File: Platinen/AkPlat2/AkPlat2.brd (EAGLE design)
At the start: 54.6 x 46.6 mm, 12 parts, among them CON1 XT30UPB-M, X1 332-02, X2 332-02, X3 332-02, X4 332-02

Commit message: platine verbessert
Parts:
- removed X1, X2, X3, X4: 332-02, con-garry:332-02
- added SV1, SV2: (no value), con-lstb:MA04-1
- moved JP4 1.38 mm to (4.60, 10.3)
- moved JP3 0.64 mm to (4.58, 17.9)
- moved JP1 0.58 mm to (4.58, 33.2)
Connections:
- net N$16: now also SV1.1; no longer X1.2
- net N$17: now also SV1.2; no longer X1.1
- net N$18: now also SV1.3; no longer X2.2
- net N$19: now also SV1.4; no longer X2.1
- net N$20: now also SV2.1; no longer X3.2
- net N$21: now also SV2.2; no longer X3.1
- net N$22: now also SV2.3; no longer X4.2
- net N$23: now also SV2.4; no longer X4.1
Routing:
- net N$8: track 48.7 -> 51.7 mm
- net N$27: track 9.62 -> 7.51 mm
- net N$24: track 103.7 -> 105.3 mm
- net N$9: track 16.6 -> 18.1 mm
- net N$11: track 22.6 -> 24.0 mm
- net N$18: track 4.32 -> 5.47 mm
- net N$23: track 3.81 -> 4.88 mm
- net N$20: track 4.50 -> 5.53 mm
- net N$17: track 4.81 -> 5.76 mm
- net N$19: track 4.83 -> 5.76 mm
- net N$16: track 4.31 -> 5.18 mm
- net N$28: track 159.1 -> 158.2 mm
- net N$21: track 3.99 -> 4.81 mm
- net N$22: track 3.91 -> 4.53 mm
- net N$7: track 8.90 -> 8.33 mm
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
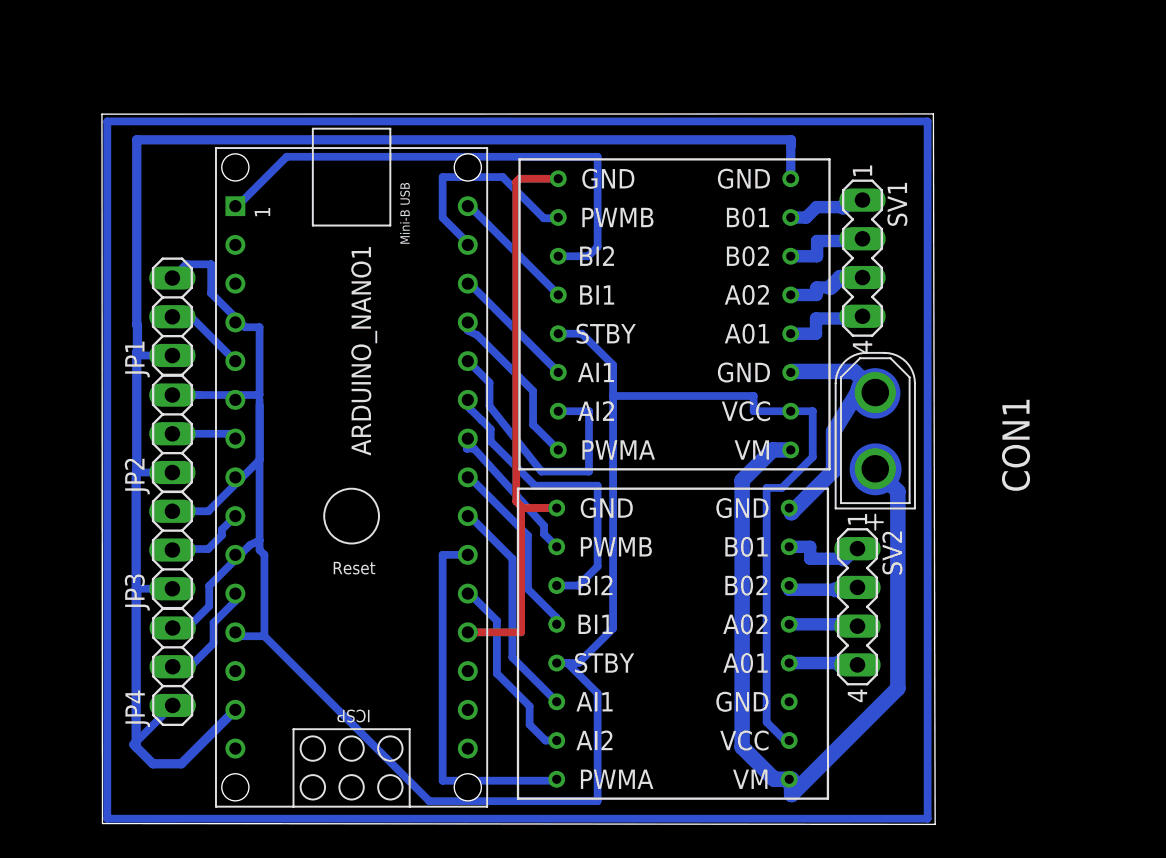
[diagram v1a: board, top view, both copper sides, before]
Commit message: Platine changes and smother movement
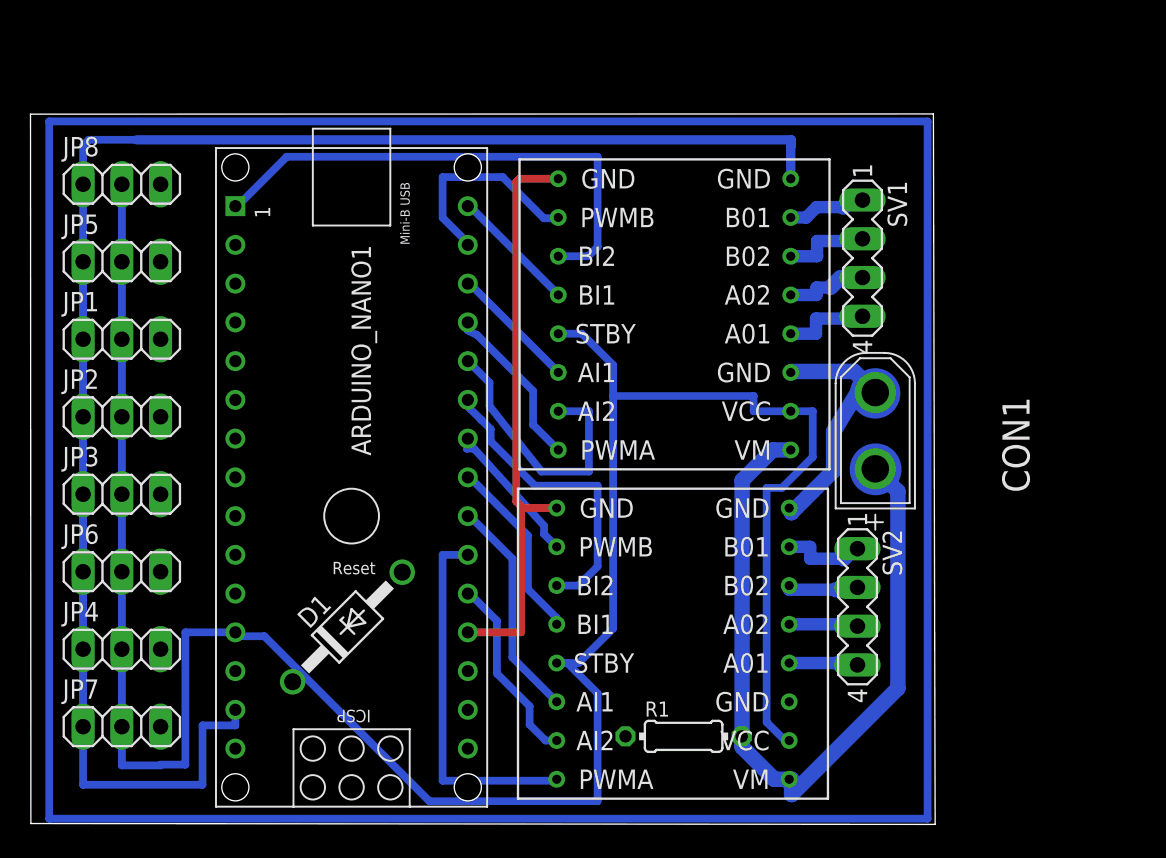
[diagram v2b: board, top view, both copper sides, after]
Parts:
- added D1: BZX85, diode:DO41Z10
- added JP5, JP6, JP7, JP8: (no value), pinhead:1X03
- added R1: (no value), rcl:0204/7
- moved JP3 4.94 mm to (1.27, 21.6), turned to 0 degrees
- moved JP1 3.63 mm to (1.27, 31.8), turned to 0 degrees
- moved JP4 3.53 mm to (1.27, 11.4), turned to 0 degrees
- moved JP2 3.50 mm to (1.27, 26.7), turned to 0 degrees
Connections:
- removed net N$24: ARDUINO_NANO1.14, JP1.1, JP2.1, JP3.1, JP4.1, U$1.1
- removed net N$25: ARDUINO_NANO1.5, JP1.2
- new net N$30: ARDUINO_NANO1.9, JP4.3
- new net N$31: ARDUINO_NANO1.8, JP3.3
- new net N$32: ARDUINO_NANO1.7, JP2.3
- new net N$33: ARDUINO_NANO1.6, JP1.3
- new net N$34: ARDUINO_NANO1.5, JP5.3
- new net N$35: ARDUINO_NANO1.4, JP8.3
- net N$1: now also D1.A
- net N$15: now also ARDUINO_NANO1.14, JP1.1, JP2.1, JP3.1, JP4.1, JP5.1, JP6.1, JP7.1, JP8.1, U$1.1; no longer ARDUINO_NANO1.7, JP2.2
- net N$26: now also ARDUINO_NANO1.11, JP7.3; no longer ARDUINO_NANO1.9, JP3.2
- net N$27: now also ARDUINO_NANO1.10, JP6.3; no longer ARDUINO_NANO1.11, JP4.2
- net N$28: now also D1.C, JP1.2, JP2.2, JP3.2, JP4.2, JP5.2, JP6.2, JP7.2, JP8.2, R1.1; no longer JP1.3, JP2.3, JP3.3, JP4.3
- net N$8: now also R1.2
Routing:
- net N$15: track 4.26 -> 136.4 mm
- net N$24: track 105.3 -> 0.00 mm
- net N$29: track 199.0 -> 206.6 mm
- net N$27: track 7.51 -> 0.00 mm
- net N$25: track 5.33 -> 0.00 mm
- net N$26: track 5.27 -> 0.00 mm
- net N$18: track 5.47 -> 4.02 mm
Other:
- board size 54.6 x 46.6 mm -> 59.3 x 46.6 mm

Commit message: Palatine new plug alignment
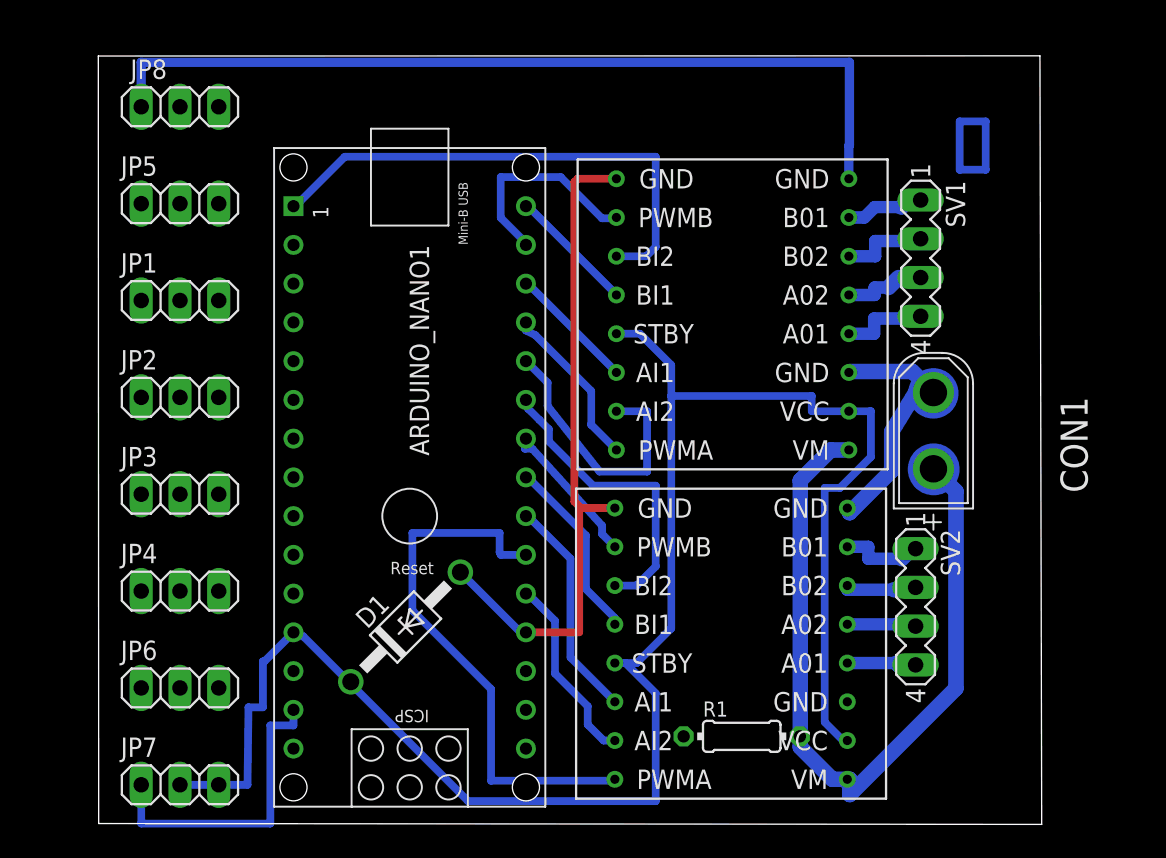
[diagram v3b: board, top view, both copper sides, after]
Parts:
- moved JP6 8.52 mm to (5.08, 8.89)
- moved JP8 6.35 mm to (5.08, 47.0)
- moved JP5 5.39 mm to (5.08, 40.6)
- moved JP4 5.39 mm to (5.08, 15.2)
- moved JP7 5.39 mm to (5.08, 2.54)
- moved JP1 4.58 mm to (5.08, 34.3)
- moved JP2 4.02 mm to (5.08, 27.9)
- moved CON1 3.81 mm to (54.5, 25.8)
- moved SV1 3.81 mm to (53.6, 37.1)
- moved SV2 3.81 mm to (53.3, 14.2)
- moved U$1 3.81 mm to (51.5, 43.5)
- moved JP3 3.81 mm to (5.08, 21.6)
- moved ARDUINO_NANO1 3.81 mm to (20.1, 20.2)
- moved D1 3.81 mm to (19.9, 12.9)
- moved R1 3.81 mm to (41.9, 5.71)
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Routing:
- net N$29: track 206.6 -> 9.75 mm
- net N$15: track 136.4 -> 77.0 mm
- net N$28: track 157.8 -> 120.3 mm
- net N$11: track 24.0 -> 35.4 mm
- net N$1: track 38.3 -> 44.3 mm
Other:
- board size 59.3 x 46.6 mm -> 61.8 x 50.4 mm

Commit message: PCB almost done
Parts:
- removed SV1, SV2: (no value), con-lstb:MA04-1
- added JP10, JP11, JP12, JP9: (no value), pinhead:1X02
- moved U$1 2.50 mm to (52.7, 45.7)
- moved CON1 2.06 mm to (56.5, 26.0)
- moved ARDUINO_NANO1 2.04 mm to (21.6, 21.6)
- moved R1 1.80 mm to (43.2, 6.99)
- moved JP1 1.80 mm to (6.35, 35.6)
- moved JP4 1.80 mm to (6.35, 16.5)
- moved JP7 1.80 mm to (6.35, 3.81)
- moved JP2 1.80 mm to (6.35, 29.2)
- moved JP3 1.80 mm to (6.35, 22.9)
- moved JP6 1.80 mm to (6.35, 10.2)
- moved JP5 1.80 mm to (6.35, 41.9)
- moved JP8 1.80 mm to (6.35, 48.3)
- moved U$2 1.61 mm to (52.7, 22.9)
- moved D1 1.53 mm to (21.0, 14.0)
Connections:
- net N$28 renamed 5V
- net N$8 renamed VM
- removed net N$1: ARDUINO_NANO1.19, D1.A, U$1.9, U$2.9
- removed net N$15: ARDUINO_NANO1.14, JP1.1, JP2.1, JP3.1, JP4.1, JP5.1, JP6.1, JP7.1, JP8.1, U$1.1
- removed net N$2: CON1.-, U$1.6, U$2.1
- new net GND: ARDUINO_NANO1.14, ARDUINO_NANO1.19, CON1.-, D1.A, JP1.1, JP2.1, JP3.1, JP4.1, JP5.1, JP6.1, JP7.1, JP8.1, U$1.1, U$1.6, U$1.9, U$2.1, U$2.6, U$2.9
- net N$16: now also JP9.1; no longer SV1.1
- net N$17: now also JP9.2; no longer SV1.2
- net N$18: now also JP10.1; no longer SV1.3
- net N$19: now also JP10.2; no longer SV1.4
- net N$20: now also JP11.1; no longer SV2.1
- net N$21: now also JP11.2; no longer SV2.2
- net N$22: now also JP12.1; no longer SV2.3
- net N$23: now also JP12.2; no longer SV2.4
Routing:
- net 5V: track 120.3 -> 5.01 mm
- net N$15: track 77.0 -> 0.00 mm
- net N$1: track 44.3 -> 0.00 mm
- net N$35: track 0.00 -> 17.2 mm
- net N$2: track 17.1 -> 0.00 mm
- net N$26: track 0.00 -> 14.8 mm
- net N$34: track 0.00 -> 13.4 mm
- net VM: track 51.7 -> 40.1 mm
- net N$27: track 0.00 -> 11.0 mm
- net N$11: track 35.4 -> 24.6 mm
- net N$29: track 9.75 -> 0.00 mm
- net N$33: track 0.00 -> 9.38 mm
- net N$23: track 4.88 -> 12.1 mm
- net N$30: track 0.00 -> 7.18 mm
- net N$32: track 0.00 -> 6.13 mm
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- added copper zone on layer 16, net 5V
- added copper zone on layer 1, net GND
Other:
- board size 61.8 x 50.4 mm -> 62.2 x 51.4 mm

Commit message: PCB fertig Gerber fertig
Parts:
- removed ARDUINO_NANO1: (no value), ArduinoNanoV30:ARDUINO_NANO
- removed CON1: XT30UPB-M, amass:XT30UPB-M
- removed D1: BZX85, diode:DO41Z10
- removed JP1, JP2, JP3, JP4, JP5, JP6, JP7, JP8: (no value), pinhead:1X03
- removed JP10, JP11, JP12, JP9: (no value), pinhead:1X02
- removed R1: (no value), rcl:0204/7
- added 1.1, 1.2, 2.1, 2.2, 3.1, 3.2, 4.1, 4.2: 22-23-2031, con-molex:22-23-2031
- added 100Ω: 100, rcl:0204/7
- added ARDUINO_NANO: (no value), ArduinoNanoV30:ARDUINO_NANO
- added M1, M2, M3, M4: 22-23-2021, con-molex:22-23-2021
- added POWER: XT30UPB-M, amass:XT30UPB-M
- added ZENER_5V1: BZX85, diode:DO41Z10
- moved U$1 1.27 mm to (54.0, 45.7)
- moved U$2 1.27 mm to (54.0, 22.9)
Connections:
- net 5V: now also 1.1.2, 1.2.2, 100Ω.1, 2.1.2, 2.2.2, 3.1.2, 3.2.2, 4.1.2, 4.2.2, ARDUINO_NANO.12, ZENER_5V1.C; no longer ARDUINO_NANO1.12, D1.C, JP1.2, JP2.2, JP3.2, JP4.2, JP5.2, JP6.2, JP7.2, JP8.2, R1.1
- net BIN2: now also ARDUINO_NANO.1; no longer ARDUINO_NANO1.1
- net GND: now also 1.1.1, 1.2.1, 2.1.1, 2.2.1, 3.1.1, 3.2.1, 4.1.1, 4.2.1, ARDUINO_NANO.14, ARDUINO_NANO.19, POWER.-, ZENER_5V1.A; no longer ARDUINO_NANO1.14, ARDUINO_NANO1.19, CON1.-, D1.A, JP1.1, JP2.1, JP3.1, JP4.1, JP5.1, JP6.1, JP7.1, JP8.1
- net N$10: now also ARDUINO_NANO.24; no longer ARDUINO_NANO1.24
- net N$11: now also ARDUINO_NANO.21; no longer ARDUINO_NANO1.21
- net N$12: now also ARDUINO_NANO.20; no longer ARDUINO_NANO1.20
- net N$13: now also ARDUINO_NANO.22; no longer ARDUINO_NANO1.22
- net N$14: now also ARDUINO_NANO.23; no longer ARDUINO_NANO1.23
- net N$16: now also M1.1; no longer JP9.1
- net N$17: now also M1.2; no longer JP9.2
- net N$18: now also M2.1; no longer JP10.1
- net N$19: now also M2.2; no longer JP10.2
- net N$20: now also M3.1; no longer JP11.1
- net N$21: now also M3.2; no longer JP11.2
- net N$22: now also M4.1; no longer JP12.1
- net N$23: now also M4.2; no longer JP12.2
- net N$26: now also 4.2.3, ARDUINO_NANO.11; no longer ARDUINO_NANO1.11, JP7.3
- net N$27: now also 4.1.3, ARDUINO_NANO.10; no longer ARDUINO_NANO1.10, JP6.3
- net N$3: now also ARDUINO_NANO.27; no longer ARDUINO_NANO1.27
- net N$30: now also 3.1.3, ARDUINO_NANO.9; no longer ARDUINO_NANO1.9, JP4.3
- net N$31: now also 3.2.3, ARDUINO_NANO.8; no longer ARDUINO_NANO1.8, JP3.3
- net N$32: now also 2.1.3, ARDUINO_NANO.7; no longer ARDUINO_NANO1.7, JP2.3
- net N$33: now also 2.2.3, ARDUINO_NANO.6; no longer ARDUINO_NANO1.6, JP1.3
- net N$34: now also 1.1.3, ARDUINO_NANO.5; no longer ARDUINO_NANO1.5, JP5.3
- net N$35: now also 1.2.3, ARDUINO_NANO.4; no longer ARDUINO_NANO1.4, JP8.3
- net N$4: now also ARDUINO_NANO.25; no longer ARDUINO_NANO1.25
- net N$5: now also ARDUINO_NANO.30; no longer ARDUINO_NANO1.30
- net N$6: now also ARDUINO_NANO.29; no longer ARDUINO_NANO1.29
- net N$7: now also ARDUINO_NANO.28; no longer ARDUINO_NANO1.28
- net N$9: now also ARDUINO_NANO.26; no longer ARDUINO_NANO1.26
- net VIN: now also ARDUINO_NANO.15; no longer ARDUINO_NANO1.15
- net VM: now also 100Ω.2, POWER.+; no longer CON1.+, R1.2
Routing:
- net VM: track 40.1 -> 54.8 mm
- net N$32: track 6.13 -> 20.3 mm
- net GND: track 0.00 -> 11.0 mm
- net N$34: track 13.4 -> 21.6 mm
- net N$26: track 14.8 -> 7.18 mm
- net N$31: track 5.61 -> 12.5 mm
- net N$27: track 11.0 -> 15.9 mm
- net N$35: track 17.2 -> 12.3 mm
- net N$33: track 9.38 -> 6.13 mm
- net N$21: track 8.30 -> 10.8 mm
- net N$20: track 8.30 -> 10.5 mm
- net N$30: track 7.18 -> 5.08 mm
- net N$19: track 6.98 -> 7.62 mm
- net N$18: track 6.98 -> 7.62 mm
- net N$23: track 12.1 -> 12.6 mm
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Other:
- board size 62.2 x 51.4 mm -> 63.5 x 47.6 mm
- board text added: "+"
- board text added: "GND"
- board text added: "Motor-Controller 4Motors 8Sensors"
- board text added: "Robotik HTL Weiz designed by Schaumi"
- board text added: "S + -"
- board text added: "VCC"

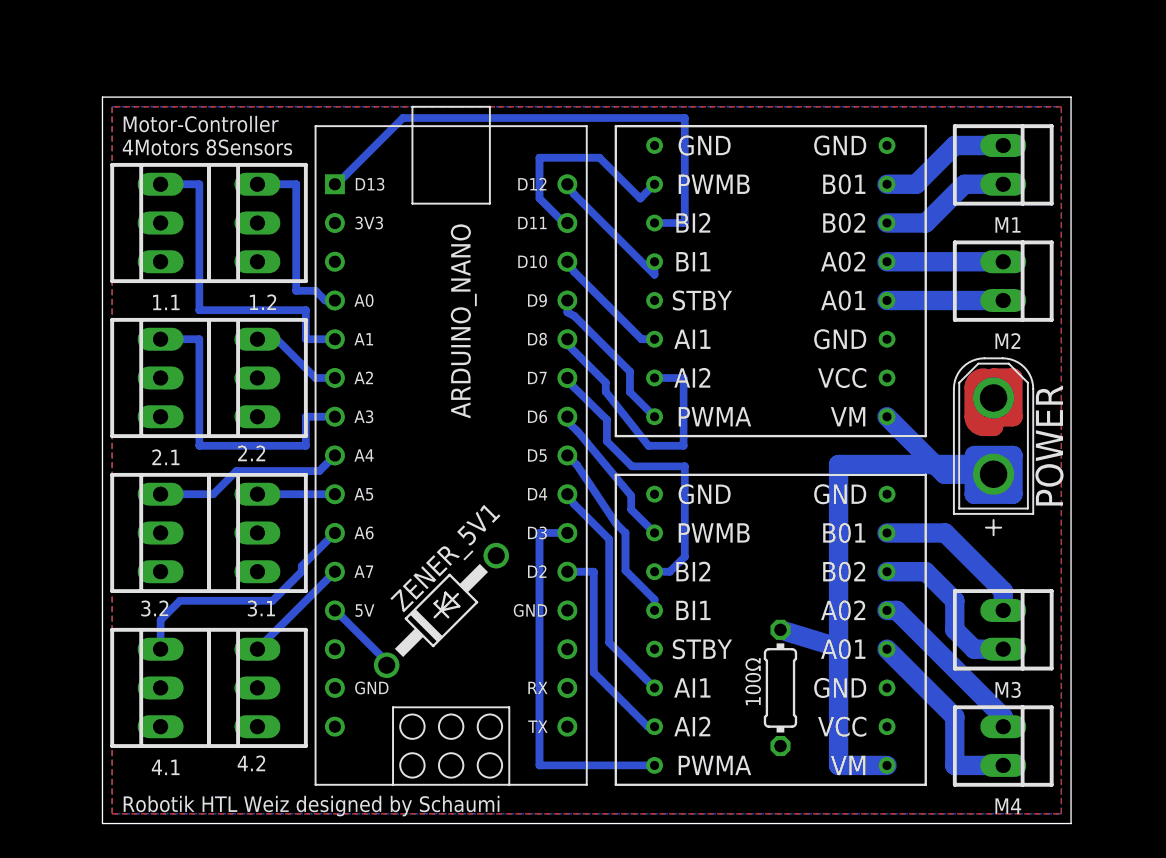
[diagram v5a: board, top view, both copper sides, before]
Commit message: Motorcontroller Platine V3.0 finished
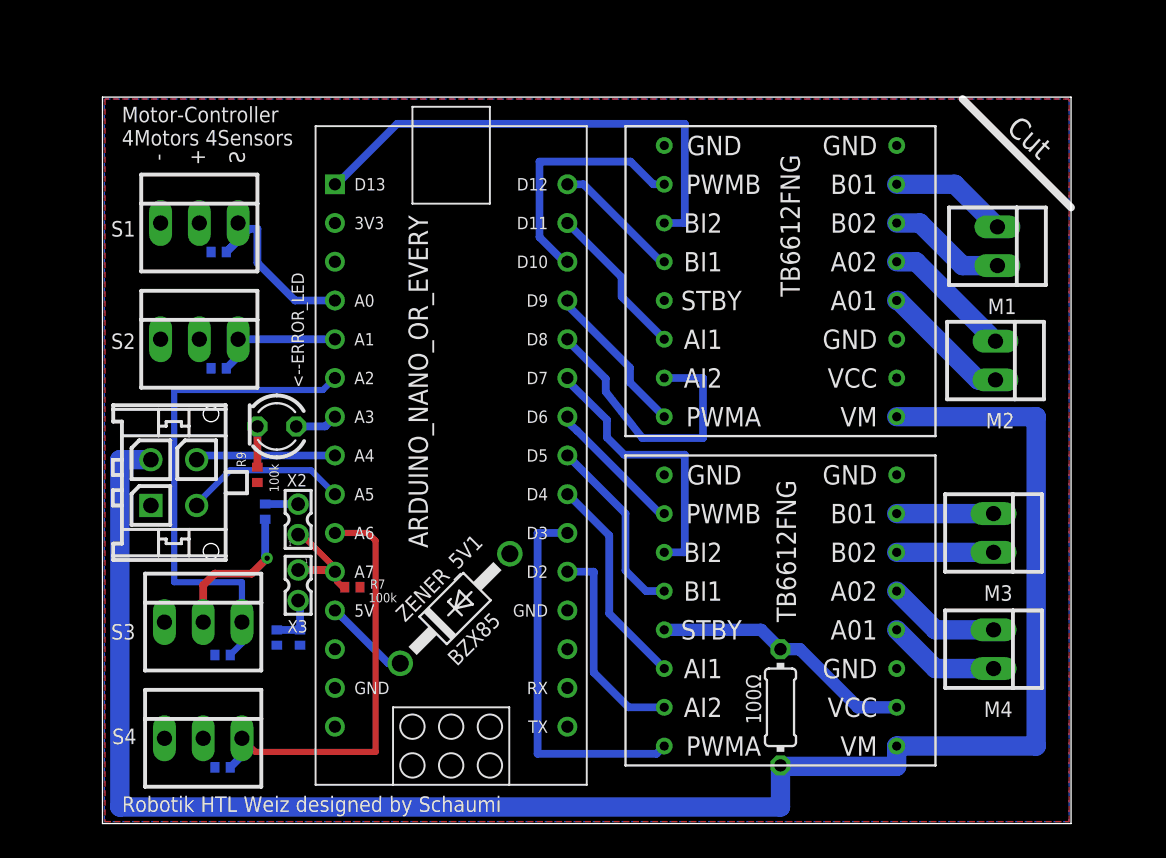
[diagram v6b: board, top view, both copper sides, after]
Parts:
- removed 1.1, 1.2, 2.1, 2.2, 3.1, 3.2, 4.1, 4.2: 22-23-2031, con-molex:22-23-2031
- removed POWER: XT30UPB-M, amass:XT30UPB-M
- added <--ERROR_LED: (no value), led:LED3MM
- added R1, R2, R3, R4, R5, R6, R7, R8, R9: 100k, rcl:R0402
- added S1, S2, S3, S4: 22-23-2031, con-molex:22-23-2031
- added X1: (no value), con-molex-micro-fit-3_0:43045-0412
- added X2, X3: 332-02, con-garry:332-02
- moved M3 6.38 mm to (58.4, 19.1)
- moved M4 6.38 mm to (58.4, 11.4)
- moved M1 5.35 mm to (58.7, 37.8)
- moved M2 5.23 mm to (58.5, 30.4)
- moved U$2 1.42 mm to (54.6, 24.1)
- moved 100Ω 1.27 mm to (44.5, 7.62), turned to 270 degrees
- moved ZENER_5V1 0.90 mm to (23.1, 14.1)
- moved U$1 0.63 mm to (54.6, 45.7)
- renumbered ARDUINO_NANO to ARDUINO_NANO_OR_EVERY
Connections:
- removed net N$27: 4.1.3, ARDUINO_NANO_OR_EVERY.10
- removed net N$30: 3.1.3, ARDUINO_NANO_OR_EVERY.9
- removed net N$31: 3.2.3, ARDUINO_NANO_OR_EVERY.8
- new net N$1: ARDUINO_NANO_OR_EVERY.8, X1.P$4
- new net N$15: R6.1, X2.2
- new net N$2: ARDUINO_NANO_OR_EVERY.9, X1.P$3
- new net N$24: R5.2, R8.2, X3.2
- new net N$25: <--ERROR_LED.A, ARDUINO_NANO_OR_EVERY.7
- new net N$8: ARDUINO_NANO_OR_EVERY.11, R7.1, X2.1, X3.1
- net 5V: now also R1.1, R2.1, R3.1, R4.1, R5.1, R6.2, R8.1, S1.2, S2.2, S3.2, S4.2; no longer 1.1.2, 1.2.2, 2.1.2, 2.2.2, 3.1.2, 3.2.2, 4.1.2, 4.2.2
- net GND: now also R7.2, R9.1, S1.1, S2.1, S3.1, S4.1, X1.P$1; no longer 1.1.1, 1.2.1, 2.1.1, 2.2.1, 3.1.1, 3.2.1, 4.1.1, 4.2.1, POWER.-
- net N$26: now also <--ERROR_LED.K, R9.2; no longer 4.2.3, ARDUINO_NANO_OR_EVERY.11
- net N$32: now also ARDUINO_NANO_OR_EVERY.10, R4.2, S4.3; no longer 2.1.3, ARDUINO_NANO_OR_EVERY.7
- net N$33: now also R3.2, S3.3; no longer 2.2.3
- net N$34: now also R2.2, S2.3; no longer 1.1.3
- net N$35: now also R1.2, S1.3; no longer 1.2.3
- net N$6: now also ARDUINO_NANO_OR_EVERY.28; no longer ARDUINO_NANO_OR_EVERY.29
- net N$7: now also ARDUINO_NANO_OR_EVERY.29; no longer ARDUINO_NANO_OR_EVERY.28
- net VM: now also X1.P$2; no longer POWER.+
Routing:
- net VM: track 54.8 -> 119.7 mm
- net 5V: track 5.01 -> 33.0 mm, vias 0 -> 1
- net N$33: track 6.13 -> 33.0 mm
- net N$27: track 15.9 -> 0.00 mm
- net N$34: track 21.6 -> 8.57 mm
- net N$31: track 12.5 -> 0.00 mm
- net GND: track 11.0 -> 0.00 mm
- net N$2: track 0.00 -> 10.7 mm
- net N$1: track 0.00 -> 9.18 mm
- net N$32: track 20.3 -> 28.1 mm
- net N$8: track 0.00 -> 7.58 mm
- net N$23: track 12.6 -> 7.40 mm
- net N$30: track 5.08 -> 0.00 mm
- net N$26: track 7.18 -> 2.68 mm
- net N$21: track 10.8 -> 6.35 mm
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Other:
- board text added: "Cut"
- board text added: "Motor-Controller 4Motors 4Sensors"
- board text added: "TB6612FNG"
- board text removed: "+"
- board text removed: "Motor-Controller 4Motors 8Sensors"
